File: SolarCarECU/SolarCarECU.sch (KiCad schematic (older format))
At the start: 101 parts, among them U1 Teensy3.6

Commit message: added optional CAN termination, added proper MOSFET driver and fixed MOSFET connections for high power devices
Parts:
- removed C?: 0.47u, Capacitors_SMD:C_0603, symbol Device:C
- removed C?: 4.7u, Capacitors_SMD:C_0603, symbol Device:C
- removed C?: 47u, Capacitors_SMD:C_0603, symbol Device:C
- removed Q? (x3): QM6015D, Package_TO_SOT_SMD:TO-252-2, symbol Transistor_FET:QM6015D
- added C? (x2): 0.47u, Capacitors_SMD:C_0603, symbol Device:C
- added C? (x3): 4.7u, Capacitors_SMD:C_0603, symbol Device:C
- added C? (x2): 47u, Capacitors_SMD:C_0603, symbol Device:C
- added Q? (x4): QM6015D, Package_TO_SOT_SMD:TO-252-2, symbol Transistor_FET:QM6015D
- added R? (x2): 120, Resistors_SMD:R_0603, symbol Device:R
- added U? (x2): EL7202CN, symbol Driver_FET:EL7202CN
- J? (x2): footprint (none) -> Connectors_Terminal_Blocks:TerminalBlock_Altech_AK300-4_P5.00mm
- J?: footprint (none) -> Connectors_Phoenix:PhoenixContact_GMSTB-GF_10x7.62mm_Angled_ThreadedFlange_MountHole
- U1: symbol teensy:Teensy3.6 -> SolarCarECU-rescue:Teensy3.6-teensy
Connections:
- net labels added: HORN, LV_HORN
- wire segments 486 -> 527

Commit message: Added teensy code for motor controller
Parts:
- C? (x35): symbol Device:C -> SolarCarECU-rescue:C-Device
- C? (x3): symbol Device:CP -> SolarCarECU-rescue:CP-Device
- D?: symbol Device:D_Zener -> SolarCarECU-rescue:D_Zener-Device
- D?: symbol Device:D_Schottky -> SolarCarECU-rescue:D_Schottky-Device
- J? (x2): symbol Connector:Screw_Terminal_01x08 -> SolarCarECU-rescue:Screw_Terminal_01x08-Connector
- J?: symbol Connector:Screw_Terminal_01x02 -> SolarCarECU-rescue:Screw_Terminal_01x02-Connector
- J? (x3): symbol Connector:Screw_Terminal_01x04 -> SolarCarECU-rescue:Screw_Terminal_01x04-Connector
- J?: symbol Connector:Screw_Terminal_01x14 -> SolarCarECU-rescue:Screw_Terminal_01x14-Connector
- J?: symbol Connector:Screw_Terminal_01x10 -> SolarCarECU-rescue:Screw_Terminal_01x10-Connector
- J?: symbol Connector:USB_B_Micro -> SolarCarECU-rescue:USB_B_Micro-Connector
- Q? (x5): symbol Transistor_FET:QM6015D -> SolarCarECU-rescue:QM6015D-Transistor_FET
- Q?: symbol Transistor_BJT:PZT2222A -> SolarCarECU-rescue:PZT2222A-Transistor_BJT
- R? (x41): symbol Device:R -> SolarCarECU-rescue:R-Device
- U? (x2): symbol Interface_CAN_LIN:MCP2562-E-P -> SolarCarECU-rescue:MCP2562-E-P-Interface_CAN_LIN
- U? (x2): symbol Driver_FET:EL7202CN -> SolarCarECU-rescue:EL7202CN-Driver_FET
- U? (x3): symbol 4xxx:4504 -> SolarCarECU-rescue:4504-4xxx
- U?: symbol Regulator_Linear:L7805 -> SolarCarECU-rescue:L7805-Regulator_Linear
- U? (x5): symbol Amplifier_Operational:LM324A -> SolarCarECU-rescue:LM324A-Amplifier_Operational

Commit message: Footprints Completed
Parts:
- removed J? (x2): Screw_Terminal_01x04, Connectors_Terminal_Blocks:TerminalBlock_Altech_AK300-4_P5.00mm, symbol SolarCarECU-rescue:Screw_Terminal_01x04-Connector
- removed J?: Screw_Terminal_01x10, Connectors_Phoenix:PhoenixContact_GMSTB-GF_10x7.62mm_Angled_ThreadedFlange_MountHole, symbol SolarCarECU-rescue:Screw_Terminal_01x10-Connector
- added J7: Screw_Terminal_01x14, Connector_PinSocket_2.54mm:PinSocket_1x14_P2.54mm_Vertical, symbol Connector:Screw_Terminal_01x14
- C1, C4: renamed from C?; footprint Capacitors_THT:CP_Radial_D13.0mm_P5.00mm -> Capacitor_THT:CP_Radial_D13.0mm_P5.00mm
- C10: renamed from C?; footprint Capacitors_Tantalum_SMD:CP_Tantalum_Case-E_EIA-7260-38_Reflow -> Capacitor_THT:CP_Radial_D13.0mm_P5.00mm
- C11, C12, C13, C14, C15, C16, C17, C18, C19, C2, C20, C21, C22, C23, C25, C26, C27, C28, C29, C3, C30, C31, C32, C34, C35, C36, C37, C38, C5, C6, C7, C8: renamed from C?; footprint Capacitors_SMD:C_0603 -> Capacitor_SMD:C_0603_1608Metric
- C24, C33: renamed from C?; footprint (none) -> Capacitor_SMD:C_0603_1608Metric
- C9: renamed from C?; footprint Capacitors_Tantalum_SMD:CP_Tantalum_Case-E_EIA-7260-38_Reflow -> Capacitor_SMD:C_0603_1608Metric
- D1, D2: renamed from D?; footprint (none) -> Diode_SMD:D_0603_1608Metric
- J1: renamed from J?; footprint Connectors_WAGO:WAGO_734_2pin_Straight_RuggedPads -> Connector_Phoenix_MC_HighVoltage:PhoenixContact_MCV_1,5_2-G-5.08_1x02_P5.08mm_Vertical
- J2: renamed from J?; footprint (none) -> SamacSys_Parts:USBRBSSOTH
- J3: renamed from J?; footprint Connectors_Terminal_Blocks:TerminalBlock_Altech_AK300-4_P5.00mm -> Connector_Phoenix_MC_HighVoltage:PhoenixContact_MCV_1,5_4-G-5.08_1x04_P5.08mm_Vertical
- J4, J5: renamed from J?; footprint Connectors_Phoenix:PhoenixContact_MC-G_08x5.08mm_Angled -> Connector_PinSocket_2.54mm:PinSocket_1x08_P2.54mm_Vertical
- J6: renamed from J?; footprint Connectors_Phoenix:PhoenixContact_MC-G_14x3.50mm_Angled -> Connector_PinSocket_2.54mm:PinSocket_1x14_P2.54mm_Vertical
- R1, R10, R11, R12, R13, R14, R15, R16, R17, R18, R19, R2, R20, R21, R22, R23, R24, R25, R26, R27, R28, R29, R3, R30, R31, R32, R33, R34, R35, R36, R37, R38, R39, R4, R40, R41, R5, R6, R7, R8, R9: renamed from R?; footprint Resistors_SMD:R_0603 -> Resistor_SMD:R_0603_1608Metric
- U1: footprint Misc:Teensy35_36 -> teensy:Teensy35_36
- U10: renamed from U?; footprint SMD_Packages:SOIC-14_N -> Package_SO:SOIC-14_3.9x8.7mm_P1.27mm
- U10: renamed from U?; footprint (none) -> Package_SO:SOIC-14_3.9x8.7mm_P1.27mm
- U2, U3: renamed from U?; footprint (none) -> Package_DIP:DIP-8_W7.62mm
- U4: renamed from U?; footprint TO_SOT_Packages_THT:TO-220-3_Horizontal -> Package_TO_SOT_THT:TO-220-3_Horizontal_TabDown
- U7, U8, U9: renamed from U?; footprint Housings_SOIC:SOIC-16_3.9x9.9mm_Pitch1.27mm -> Package_SO:SOIC-16_3.9x9.9mm_P1.27mm
- gave numbers to parts that had none: 8
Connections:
- net labels added: +12V-power, +5V-power
- wire segments 527 -> 517

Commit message: begun layout of PCB
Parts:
- J7: symbol Connector:Screw_Terminal_01x14 -> SolarCarECU-rescue:Screw_Terminal_01x14-Connector
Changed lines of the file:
@@
 Connection ~ 11000 4200
 $Comp
-L Connector:Screw_Terminal_01x14 J7
+L SolarCarECU-rescue:Screw_Terminal_01x14-Connector J7
 U 1 1 5CA6D055
 P 21400 9300

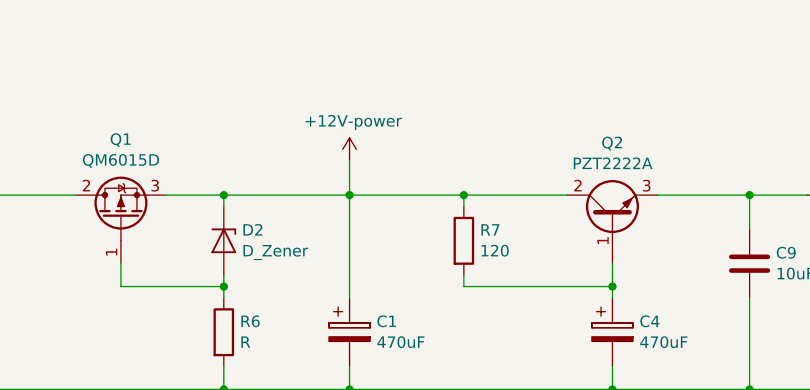
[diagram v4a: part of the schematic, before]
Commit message: Component Layout MC
MOSFET Driver, Level Shifter, OpAmp
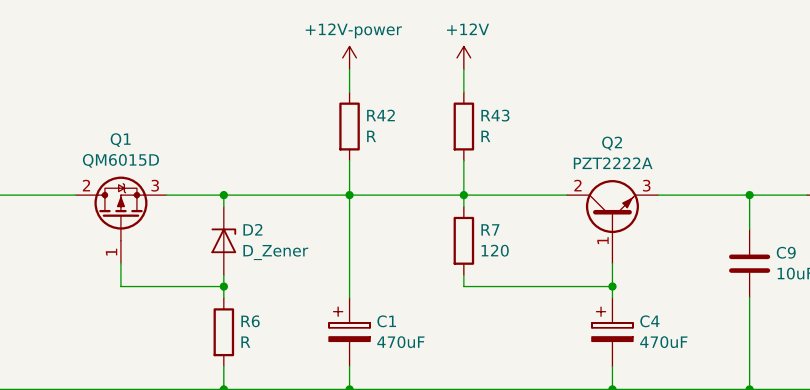
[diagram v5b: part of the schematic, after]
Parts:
- added R42, R43: R, Resistor_SMD:R_0603_1608Metric, symbol SolarCarECU-rescue:R-Device
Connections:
- net +12V: now also R42.1, R43.1; no longer C1.1, D2.1 (K), Q1.3 (S), Q2.2 (C), R7.1
- new net: C1.1, D2.1 (K), Q1.3 (S), Q2.2 (C), R42.2, R43.2, R7.1
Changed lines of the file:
@@
 L SolarCarECU-rescue:+12V-power #PWR0137
 U 1 1 5D1C1470
-P 4200 2400
-F 0 "#PWR0137" H 4200 2250 50  0001 C CNN
-F 1 "+12V-power" H 4215 2573 50  0000 C CNN
-F 2 "" H 4200 2400 50  0001 C CNN
-F 3 "" H 4200 2400 50  0001 C CNN
-	1    4200 2400
+P 4200 2000
+F 0 "#PWR0137" H 4200 1850 50  0001 C CNN
+F 1 "+12V-power" H 4215 2173 50  0000 C CNN
+F 2 "" H 4200 2000 50  0001 C CNN
+F 3 "" H 4200 2000 50  0001 C CNN
+	1    4200 2000
 	1    0    0    -1
 $EndComp
@@
 	5000 10500 5100 10500
 Connection ~ 4900 5000
-Connection ~ 4700 2550
 Connection ~ 5350 3400
-Connection ~ 3650 2550
 Connection ~ 3650 3400
 Wire Wire Line
@@
 Wire Wire Line
 	21050 9000 21200 9000
+Connection ~ 3650 2550
+Connection ~ 4700 2550
+$Comp
+L power:+12V #PWR0160
+U 1 1 5C8BE540
+P 4700 2000
+F 0 "#PWR0160" H 4700 1850 50  0001 C CNN
+F 1 "+12V" H 4715 2173 50  0000 C CNN
+F 2 "" H 4700 2000 50  0001 C CNN
+F 3 "" H 4700 2000 50  0001 C CNN
+	1    4700 2000
+	1    0    0    -1
+$EndComp
+Wire Wire Line
+	4700 2400 4700 2550
+$Comp
+L SolarCarECU-rescue:R-Device R43
+U 1 1 5C90863D
+P 4700 2250
+F 0 "R43" H 4770 2296 50  0000 L CNN
+F 1 "R" H 4770 2205 50  0000 L CNN
+F 2 "Resistor_SMD:R_0603_1608Metric" V 4630 2250 50  0001 C CNN
+F 3 "~" H 4700 2250 50  0001 C CNN
+	1    4700 2250
+	1    0    0    -1
+$EndComp
+$Comp
+L SolarCarECU-rescue:R-Device R42
+U 1 1 5C90872F
+P 4200 2250
+F 0 "R42" H 4270 2296 50  0000 L CNN
+F 1 "R" H 4270 2205 50  0000 L CNN
+F 2 "Resistor_SMD:R_0603_1608Metric" V 4130 2250 50  0001 C CNN
+F 3 "~" H 4200 2250 50  0001 C CNN
+	1    4200 2250
+	1    0    0    -1
+$EndComp
+Wire Wire Line
+	4200 2100 4200 2000
+Wire Wire Line
+	4700 2000 4700 2100
 $EndSCHEMATC

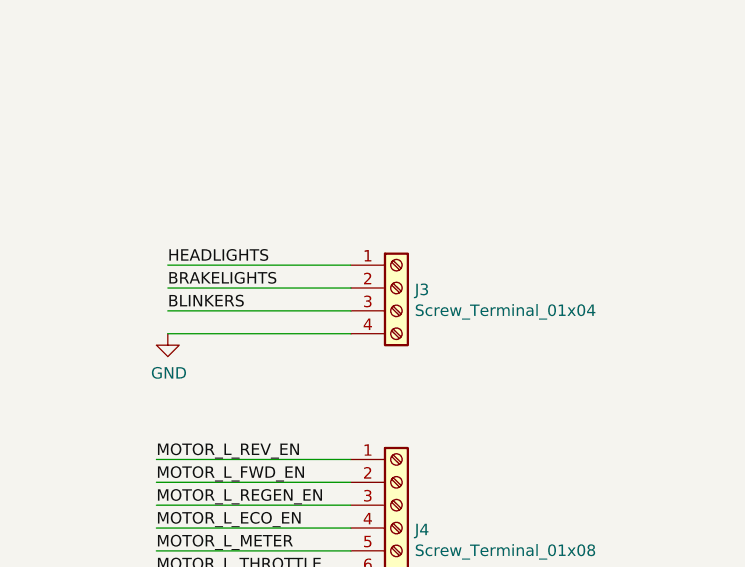
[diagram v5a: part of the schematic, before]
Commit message: Motor controller Routing
GND Vias not completed.
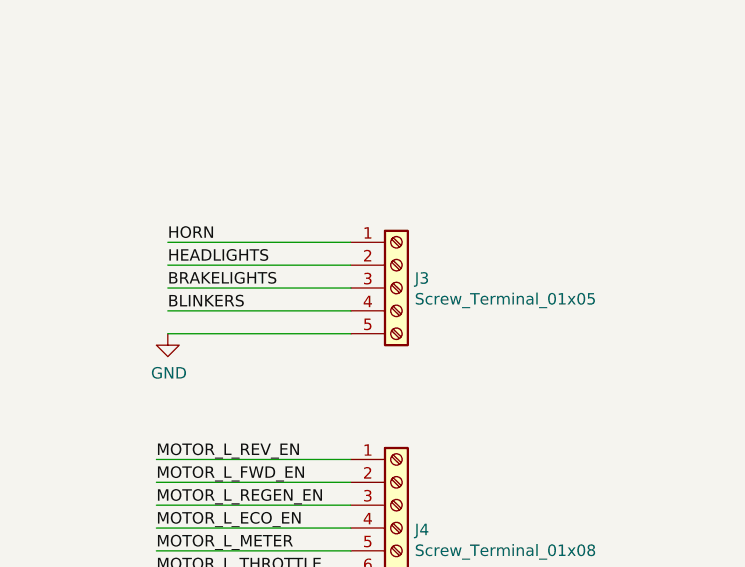
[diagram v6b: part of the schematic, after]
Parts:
- removed J3: Screw_Terminal_01x04, Connector_Phoenix_MC_HighVoltage:PhoenixContact_MCV_1,5_4-G-5.08_1x04_P5.08mm_Vertical, symbol SolarCarECU-rescue:Screw_Terminal_01x04-Connector
- added J3: Screw_Terminal_01x05, Connector_Phoenix_MC_HighVoltage:PhoenixContact_MCV_1,5_5-G-5.08_1x05_P5.08mm_Vertical, symbol Connector:Screw_Terminal_01x05
- D1, D2: footprint Diode_SMD:D_0603_1608Metric -> Diode_SMD:D_SOD-123
- U4: footprint Package_TO_SOT_THT:TO-220-3_Horizontal_TabDown -> PCBDesign:PT78NR112H
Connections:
- net BLINKERS: now also J3.4 (Pin_4)
- net BRAKELIGHTS: now also J3.3 (Pin_3)
- net GND: now also J3.5 (Pin_5)
- net HEADLIGHTS: now also J3.2 (Pin_2)
- net HORN: now also J3.1 (Pin_1)
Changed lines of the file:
@@
 F 0 "U4" H 6500 2792 50  0000 C CNN
 F 1 "L7805" H 6500 2701 50  0000 C CNN
-F 2 "Package_TO_SOT_THT:TO-220-3_Horizontal_TabDown" H 6525 2400 50  0001 L CIN
+F 2 "PCBDesign:PT78NR112H" H 6525 2400 50  0001 L CIN
 F 3 "http://www.st.com/content/ccc/resource/technical/document/datasheet/41/4f/b3/b0/12/d4/47/88/CD00000444.pdf/files/CD00000444.pdf/jcr:content/translations/en.CD00000444.pdf" H 6500 2500 50  0001 C CNN
 	1    6500 2550
@@
 F 0 "D2" V 3604 2829 50  0000 L CNN
 F 1 "D_Zener" V 3695 2829 50  0000 L CNN
-F 2 "Diode_SMD:D_0603_1608Metric" H 3650 2750 50  0001 C CNN
+F 2 "Diode_SMD:D_SOD-123" H 3650 2750 50  0001 C CNN
 F 3 "~" H 3650 2750 50  0001 C CNN
 	1    3650 2750
@@
 Text Label 20450 3150 0    50   ~ 0
 HEADLIGHTS
-$Comp
-L SolarCarECU-rescue:Screw_Terminal_01x04-Connector J3
-U 1 1 5D6FB742
-P 21450 3250
-F 0 "J3" H 21530 3242 50  0000 L CNN
-F 1 "Screw_Terminal_01x04" H 21530 3151 50  0000 L CNN
-F 2 "Connector_Phoenix_MC_HighVoltage:PhoenixContact_MCV_1,5_4-G-5.08_1x04_P5.08mm_Vertical" H 21450 3250 50  0001 C CNN
-F 3 "~" H 21450 3250 50  0001 C CNN
-	1    21450 3250
-	1    0    0    -1
-$EndComp
 $Comp
 L SolarCarECU-rescue:GND-power #PWR0141
@@
 F 0 "D1" H 3000 4084 50  0000 C CNN
 F 1 "D_Schottky" H 3000 4175 50  0000 C CNN
-F 2 "Diode_SMD:D_0603_1608Metric" H 3000 4300 50  0001 C CNN
+F 2 "Diode_SMD:D_SOD-123" H 3000 4300 50  0001 C CNN
 F 3 "~" H 3000 4300 50  0001 C CNN
 	1    3000 4300
@@
 Wire Wire Line
 	4700 2000 4700 2100
+$Comp
+L Connector:Screw_Terminal_01x05 J3
+U 1 1 5C84D545
+P 21450 3250
+F 0 "J3" H 21530 3292 50  0000 L CNN
+F 1 "Screw_Terminal_01x05" H 21530 3201 50  0000 L CNN
+F 2 "Connector_Phoenix_MC_HighVoltage:PhoenixContact_MCV_1,5_5-G-5.08_1x05_P5.08mm_Vertical" H 21450 3250 50  0001 C CNN
+F 3 "~" H 21450 3250 50  0001 C CNN
+	1    21450 3250
+	1    0    0    -1
+$EndComp
+Wire Wire Line
+	21250 3050 20450 3050
+Text Label 20450 3050 0    50   ~ 0
+HORN
 $EndSCHEMATC

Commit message: MC Routing
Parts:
- added C39, C40: C, Capacitor_SMD:C_0603_1608Metric, symbol SolarCarECU-rescue:C-Device
- added R44, R45, R46, R47: R, Resistor_SMD:R_0603_1608Metric, symbol SolarCarECU-rescue:R-Device
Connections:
- net GNDA: now also C39.2, C40.2, R45.2, R47.2
- net LV_MOTOR_L_ECO_EN: now also U1.78 (49_A23)
- net LV_MOTOR_L_FWD_EN: now also U1.69 (42)
- net LV_MOTOR_L_REGEN_EN: now also U1.79 (50_A24)
- net LV_MOTOR_L_REV_EN: now also U1.83 (54_CS2)
- net LV_MOTOR_R_ECO_EN: now also U1.36 (39_A20)
- net LV_MOTOR_R_FWD_EN: now also U1.81 (52_MOSI2)
- net LV_MOTOR_R_REGEN_EN: now also U1.82 (53_SCK2)
- net LV_MOTOR_R_REV_EN: now also U1.80 (51_MISO2)
- net MOTOR_L_ECO_EN: now also J5.5 (Pin_5); no longer J4.4 (Pin_4)
- net MOTOR_L_FWD_EN: now also J4.4 (Pin_4); no longer J4.2 (Pin_2)
- net MOTOR_L_METER: now also J4.6 (Pin_6), R46.1; no longer J4.5 (Pin_5)
- net MOTOR_L_REGEN: now also J4.3 (Pin_3); no longer J4.7 (Pin_7)
- net MOTOR_L_REGEN_EN: now also J5.4 (Pin_4); no longer J4.3 (Pin_3)
- net MOTOR_L_REV_EN: now also J4.5 (Pin_5); no longer J4.1 (Pin_1)
- net MOTOR_L_THROTTLE: now also J4.2 (Pin_2); no longer J4.6 (Pin_6)
- net MOTOR_R_ECO_EN: now also J5.1 (Pin_1); no longer J5.4 (Pin_4)
- net MOTOR_R_FWD_EN: now also J5.3 (Pin_3); no longer J5.2 (Pin_2)
- net MOTOR_R_METER: now also J4.7 (Pin_7), R44.1; no longer J5.5 (Pin_5)
- net MOTOR_R_REGEN: now also J4.1 (Pin_1); no longer J5.7 (Pin_7)
- net MOTOR_R_REGEN_EN: now also J5.2 (Pin_2); no longer J5.3 (Pin_3)
- net MOTOR_R_REV_EN: now also J5.6 (Pin_6); no longer J5.1 (Pin_1)
- net MOTOR_R_THROTTLE: now also J5.7 (Pin_7); no longer J5.6 (Pin_6)
- net PWM_MOTOR_R_REGEN: now also U1.34 (37_A18_PWM_SCL1); no longer U1.35 (38_A19_PWM_SDA1)
- net PWM_MOTOR_R_THROTTLE: now also U1.35 (38_A19_PWM_SDA1); no longer U1.34 (37_A18_PWM_SCL1)
- net LV_MOTOR_R_METER: now reaches U1.56 (A10)
- net LV_MOTOR_R_METER: now also C39.1, R44.2, R45.1
- net LV_MOTOR_L_METER: now reaches U1.57 (A11)
- net LV_MOTOR_L_METER: now also C40.1, R46.2, R47.1
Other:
- moved on the sheet: C21, C30, C35, C37, C38, R13, R19, R29, R31, R41
